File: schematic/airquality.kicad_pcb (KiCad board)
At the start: 2 copper layers, 40 x 98 mm, 55 parts, among them J1 TYPE-C-31-M-12, Q1 BC817, Q2 BC817, U1 ESP32-WROOM-32D, U2 BME280, U3 SN74LV1T34DCK, U4 SGP30, U5 TLV70218_SOT23-5, U6 PMS7003, U7 AMS1117-3.3, U8 CH340C, U9 SCD30

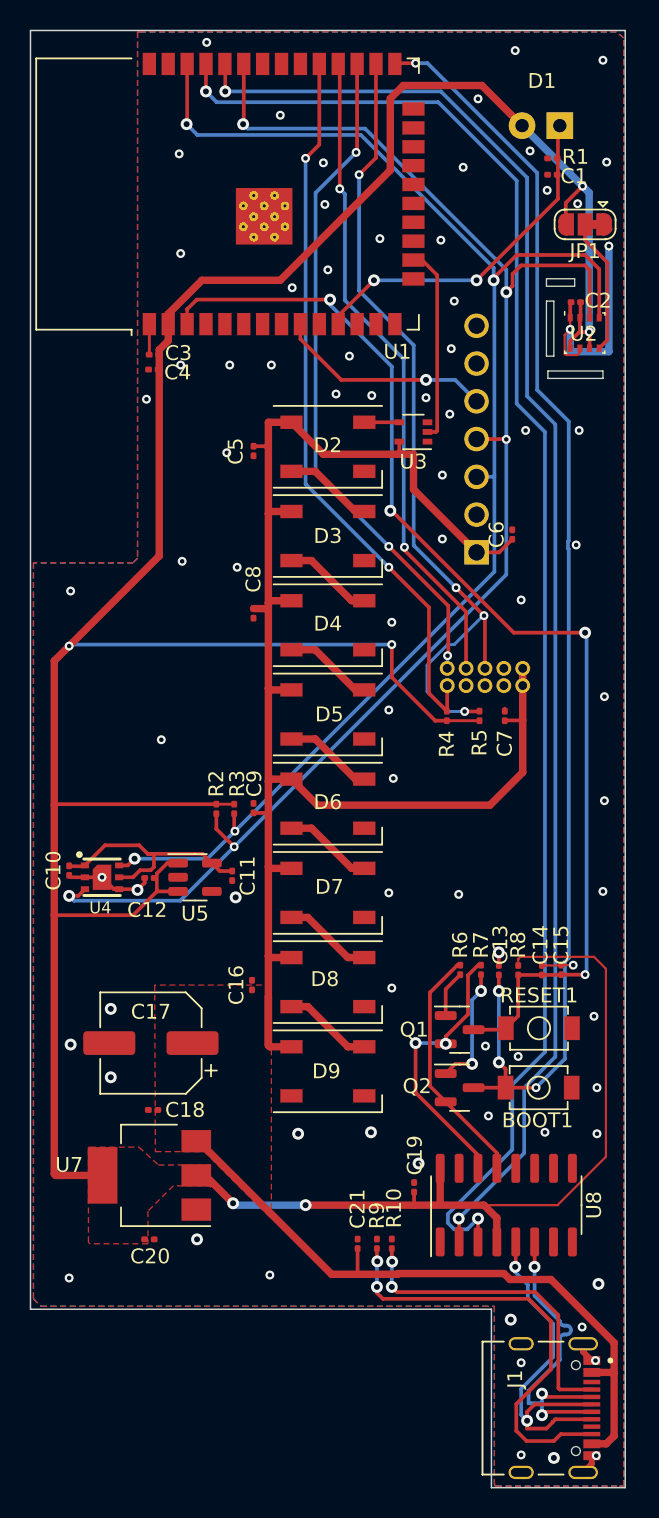
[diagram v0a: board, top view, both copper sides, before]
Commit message: Fix iluminance pin, add caps, add optional double pullups for I2C, cleaup
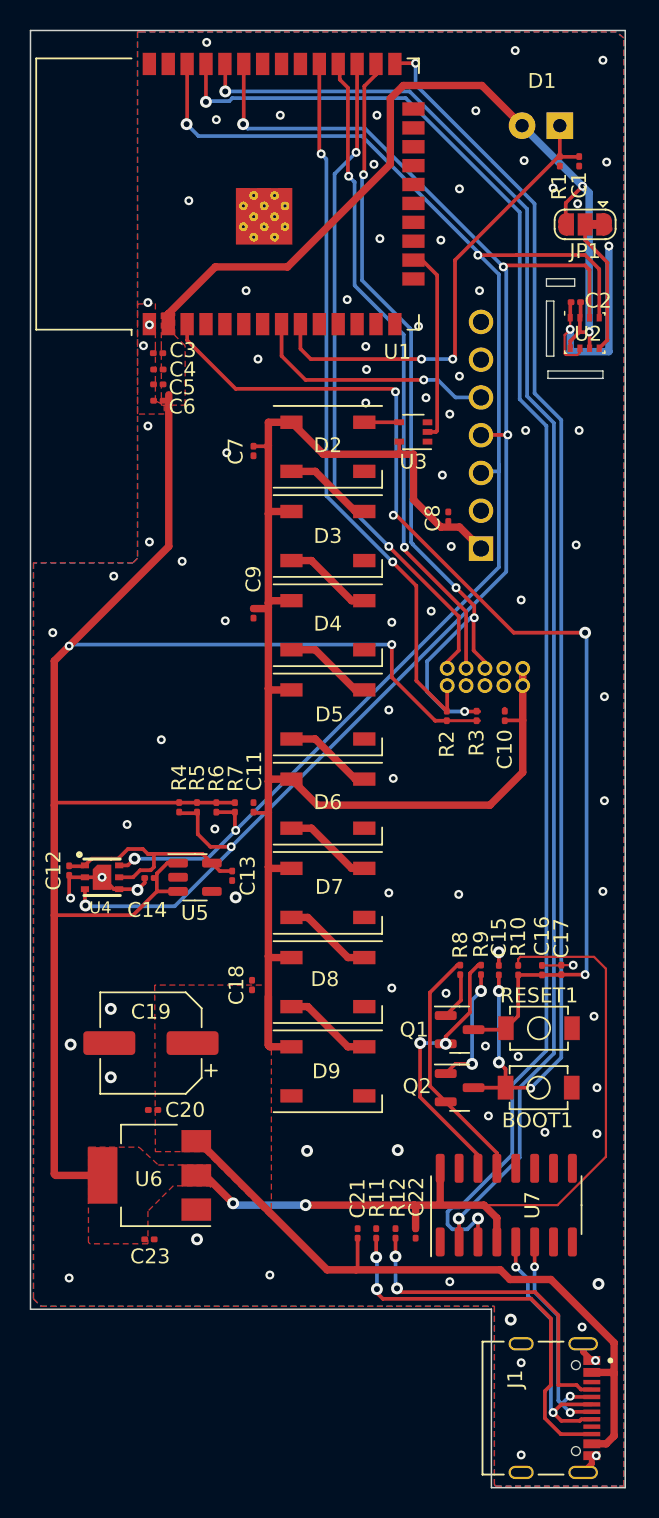
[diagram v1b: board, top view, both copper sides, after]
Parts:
- removed the U9 at (85.9, 65.0)
- added C5: 100nF, Capacitor_SMD:C_0201_0603Metric, F.Cu at (74.6, 69.8)
- added C6: 100nF, Capacitor_SMD:C_0201_0603Metric, F.Cu at (74.6, 70.9)
- added R4: 10K, Resistor_SMD:R_0201_0603Metric, F.Cu at (76.0, 98.2)
- added R6: 10K, Resistor_SMD:R_0201_0603Metric, F.Cu at (78.5, 98.2)
- added SCD30: SCD30 (CO2), symbols:MODULE_SCD30, B.Cu at (86.2, 64.7)
- moved C8 4.46 mm to (94.1, 78.7)
- moved C22 3.10 mm to (91.9, 126.9), turned to -90 degrees
- moved C1 2.01 mm to (102.9, 54.8), turned to -90 degrees
- moved R5 1.30 mm to (77.2, 98.2)
- moved R12 0.74 mm to (90.5, 126.9)
- moved R11 0.70 mm to (89.2, 126.9)
- moved C21 0.70 mm to (88.0, 126.9)
- moved R1 0.54 mm to (101.6, 54.8), turned to -90 degrees
- moved C4 0.34 mm to (74.6, 68.8)
- moved C3 0.30 mm to (74.6, 67.7)
- moved R3 0.20 mm to (96.0, 92.1)
- moved R7 0.12 mm to (79.8, 98.2)
- renumbered C7 to C10, C9 to C11, C10 to C12, C11 to C13, C12 to C14, C13 to C15, C14 to C16, C15 to C17, C16 to C18, C17 to C19, C18 to C20, C19 to C22, C20 to C23, C5 to C7, C6 to C8, C8 to C9, R8 to R10, R9 to R11, R10 to R12, R4 to R2, R5 to R3, R2 to R5, R3 to R7, R6 to R8, R7 to R9, U7 to U6, U8 to U7, U6 to U9
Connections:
- U1 pad 11: Iluminance -> unconnected-(U1-IO26-Pad11)
- U1 pad 8: unconnected-(U1-IO32-Pad8) -> SCD30_RDY
- U1 pad 9: SCD30_RDY -> Iluminance
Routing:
- net Iluminance: track 22.8 -> 31.6 mm
- net /D-: track 22.6 -> 16.1 mm
- net /D+: track 24.6 -> 18.2 mm
- net +3V3: track 231.7 -> 228.9 mm
- net Net-(J1-CC2): track 29.3 -> 26.6 mm
- net SCL: track 96.5 -> 98.8 mm
- net ESP_EN: track 76.9 -> 74.7 mm
- net SCD30_RDY: track 14.6 -> 16.7 mm
- net VBUS: track 151.7 -> 150.0 mm
- net ESP_RX: track 99.6 -> 98.3 mm
- net ESP_IO0: track 87.9 -> 86.8 mm
- net GND: track 30.6 -> 29.9 mm, vias 80 -> 88
- net PMS_SET: track 49.4 -> 48.6 mm
- net PMS_RESET: track 55.7 -> 55.0 mm
- net PMS_TX: track 45.5 -> 45.1 mm, vias 3 -> 2

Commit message: Lots of fixes
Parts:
- removed the C16 at (100.4, 109.2)
- removed J1: TYPE-C-31-M-12, symbols:HRO_TYPE-C-31-M-12
- removed U9: PMS7003, symbols:PMS7003
- added U8: PMS7003, airquality_footprints:PMS7003, B.Cu at (86.1, 107.0)
- added USB1: USB_C_Receptacle, airquality_footprints:Hanbo Electronic MC-802YC-H100, F.Cu at (86.0, 139.0)
- BOOT1, RESET1: footprint symbols:GT-TC029B-H025-L1N -> airquality_footprints:GT-TC029B-H025-L1N
- C1, C10, C11, C13, C15, C2, C3, C4, C5, C6, C7, C8, C9: footprint Capacitor_SMD:C_0201_0603Metric -> Capacitor_SMD:C_0603_1608Metric
- C12: renamed from C14; footprint Capacitor_SMD:C_0201_0603Metric -> Capacitor_SMD:C_0603_1608Metric
- C14: renamed from C12; footprint Capacitor_SMD:C_0201_0603Metric -> Capacitor_SMD:C_0603_1608Metric
- C16: renamed from C17; footprint Capacitor_SMD:C_0201_0603Metric -> Capacitor_SMD:C_0603_1608Metric
- C17: renamed from C18; footprint Capacitor_SMD:C_0201_0603Metric -> Capacitor_SMD:C_0603_1608Metric
- C19: renamed from C20; footprint Capacitor_SMD:C_0201_0603Metric -> Capacitor_SMD:C_0603_1608Metric
- C20: renamed from C21; footprint Capacitor_SMD:C_0201_0603Metric -> Capacitor_SMD:C_0603_1608Metric
- C21: renamed from C22; footprint Capacitor_SMD:C_0201_0603Metric -> Capacitor_SMD:C_0603_1608Metric
- C22: renamed from C23; footprint Capacitor_SMD:C_0201_0603Metric -> Capacitor_SMD:C_0603_1608Metric
- D1: footprint LED_THT:LED_D5.0mm_Horizontal_O6.35mm_Z15.0mm -> airquality_footprints:ALS-PDIC243-3B
- R1, R10, R11, R12, R4, R5, R6, R7, R8, R9: footprint Resistor_SMD:R_0201_0603Metric -> Resistor_SMD:R_0603_1608Metric
- R2: renamed from R3; footprint Resistor_SMD:R_0201_0603Metric -> Resistor_SMD:R_0603_1608Metric
- R3: renamed from R2; footprint Resistor_SMD:R_0201_0603Metric -> Resistor_SMD:R_0603_1608Metric
- SCD1: renamed from SCD30; footprint symbols:MODULE_SCD30 -> airquality_footprints:MODULE_SCD30
- U1: footprint RF_Module:ESP32-WROOM-32D -> airquality_footprints:ESP32-WROOM-32D
- U4: footprint symbols:SGP30 -> airquality_footprints:SGP30
- moved U4 8.30 mm to (79.0, 104.3)
- moved C14 7.73 mm to (76.1, 104.4)
- moved U5 5.97 mm to (71.3, 104.3)
- moved C13 5.38 mm to (74.4, 104.4)
- moved C20 3.90 mm to (84.1, 127.0)
- moved R4 3.51 mm to (72.5, 98.0)
- moved C12 3.04 mm to (71.3, 101.6), turned to 0 degrees
- moved R8 2.91 mm to (92.0, 109.0)
- moved R5 2.71 mm to (74.5, 98.0)
- moved C1 2.66 mm to (100.3, 55.4)
- moved R11 2.65 mm to (86.6, 127.0)
- moved R9 2.31 mm to (94.0, 109.0)
- moved R6 2.02 mm to (76.5, 98.0)
- moved C16 1.71 mm to (100.0, 109.0)
- moved C6 1.60 mm to (74.6, 72.5)
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- renumbered C19 to C18
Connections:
- U5 pad 4: unconnected-(U5-NC-Pad4) -> GND
- U7 pad 5: /D+ -> D+
- U7 pad 6: /D- -> D-
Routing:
- net D-: track 0.00 -> 22.1 mm
- net D+: track 0.00 -> 22.1 mm
- net /D+: track 18.2 -> 0.00 mm, vias 2 -> 0
- net +3V3: track 228.9 -> 211.1 mm, vias 6 -> 8
- net VBUS: track 150.0 -> 166.5 mm, vias 0 -> 2
- net /D-: track 16.1 -> 0.00 mm, vias 3 -> 0
- net Net-(USB1-CC1): track 26.6 -> 11.1 mm, vias 2 -> 1
- net GND: track 29.9 -> 20.4 mm, vias 88 -> 91
- net Net-(USB1-CC2): track 22.1 -> 13.4 mm, vias 2 -> 1
- net +1V8: track 15.7 -> 9.65 mm, vias 0 -> 2
- net PMS_RESET: track 55.0 -> 59.7 mm, vias 4 -> 3
- net ESP_EN: track 74.7 -> 71.3 mm, vias 4 -> 2
- net SDA: track 101.3 -> 98.0 mm
- net SCL: track 98.8 -> 95.8 mm, vias 4 -> 3
- net Net-(Q1-E): track 18.2 -> 19.2 mm
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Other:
- outline, holes or cut-outs redrawn

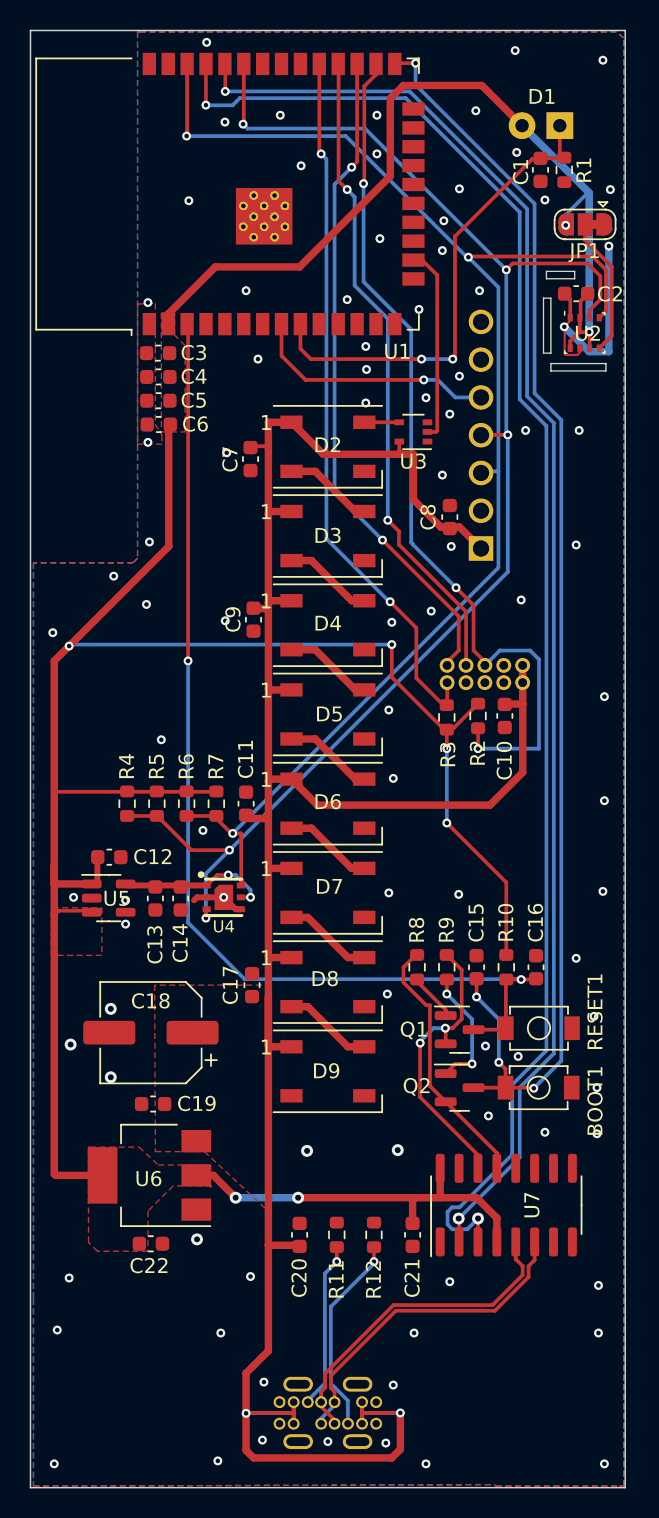
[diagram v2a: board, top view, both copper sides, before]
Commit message: swap PMS7003 with PMS5003
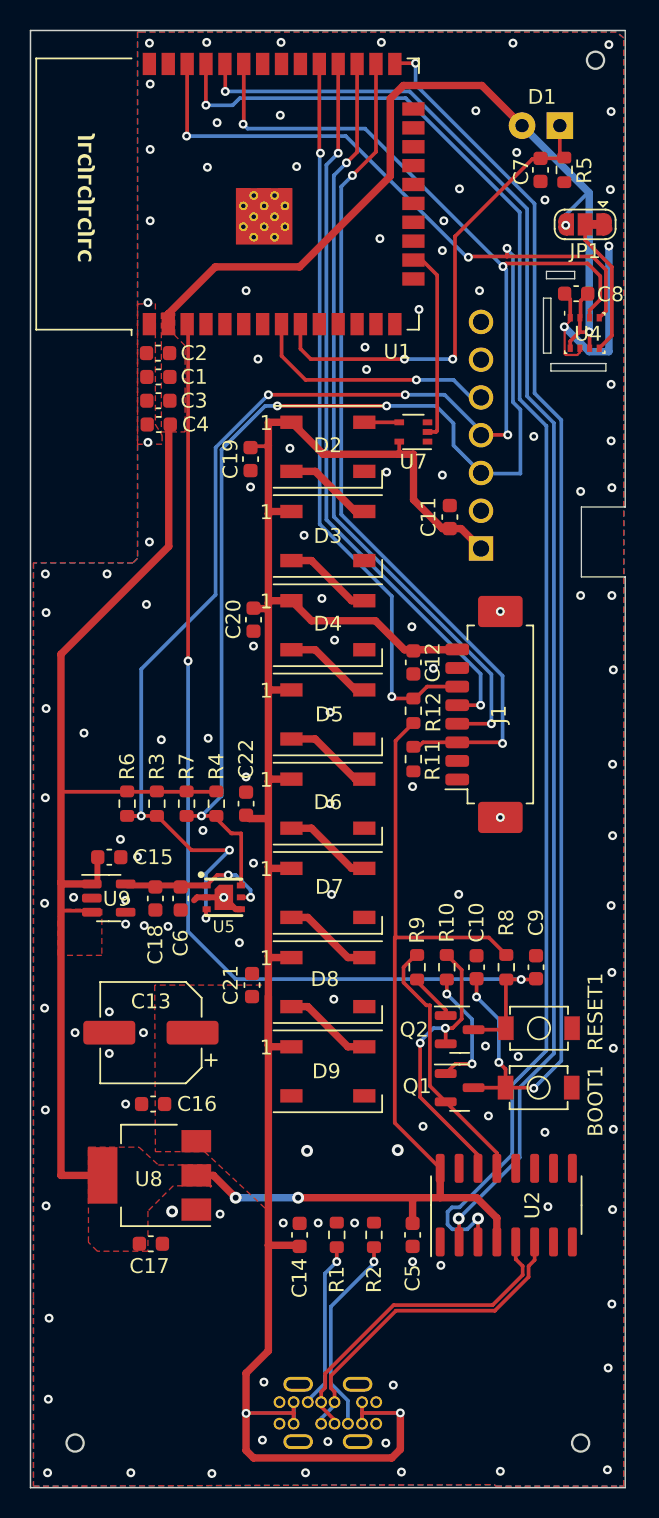
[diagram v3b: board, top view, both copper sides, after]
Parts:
- removed the U8 at (86.1, 107.0)
- added J1: Conn_01x08_MountingPin, Connector_Molex:Molex_PicoBlade_53261-0871_1x08-1MP_P1.25mm_Horizontal, F.Cu at (97.1, 92.0)
- added U6: PMS5003, airquality_footprints:PMS5003, B.Cu at (105.0, 133.0)
- moved C12 7.13 mm to (91.8, 88.5)
- moved R11 5.23 mm to (91.8, 95.0)
- moved R12 2.29 mm to (91.8, 91.8)
- renumbered C4 to C1, C15 to C10, C8 to C11, C10 to C12, C18 to C13, C20 to C14, C12 to C15, C19 to C16, C22 to C17, C13 to C18, C7 to C19, C3 to C2, C9 to C20, C17 to C21, C11 to C22, C5 to C3, C6 to C4, C21 to C5, C14 to C6, C1 to C7, C2 to C8, C16 to C9, Q2 to Q1, Q1 to Q2, R11 to R1, R9 to R10, R2 to R11, R3 to R12, R12 to R2, R5 to R3, R7 to R4, R1 to R5, R4 to R6, R6 to R7, R10 to R8, R8 to R9, U7 to U2, U2 to U4, U4 to U5, U3 to U7, U6 to U8, U5 to U9
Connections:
- R11 pad 1: +3V3 -> PMS_RESET
- R11 pad 2: PMS_RESET -> GND
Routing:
- net SCL: track 95.8 -> 113.1 mm, vias 3 -> 6
- net VBUS: track 166.5 -> 153.6 mm
- net SDA: track 98.0 -> 110.6 mm, vias 5 -> 8
- net +3V3: track 211.1 -> 199.0 mm, vias 8 -> 4
- net PMS_TX: track 44.6 -> 51.7 mm
- net PMS_RX: track 44.0 -> 49.3 mm
- net PMS_RESET: track 59.7 -> 57.3 mm, vias 3 -> 2
- net PMS_SET: track 48.0 -> 49.2 mm
- net SCD30_RDY: track 16.7 -> 16.0 mm
- net GND: vias 91 -> 127
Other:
- outline, holes or cut-outs redrawn
- board text added: "JLCJLCJLCJLC"
